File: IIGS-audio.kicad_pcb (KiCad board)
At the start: 2 copper layers, 65.8 x 46.6 mm, 39 parts, among them J1 Conn_01x07, J2 Conn_01x02_Male, J3 SJ1-3515N, J4 AppleII_slot, U1 74HC4052D, U2 TL074

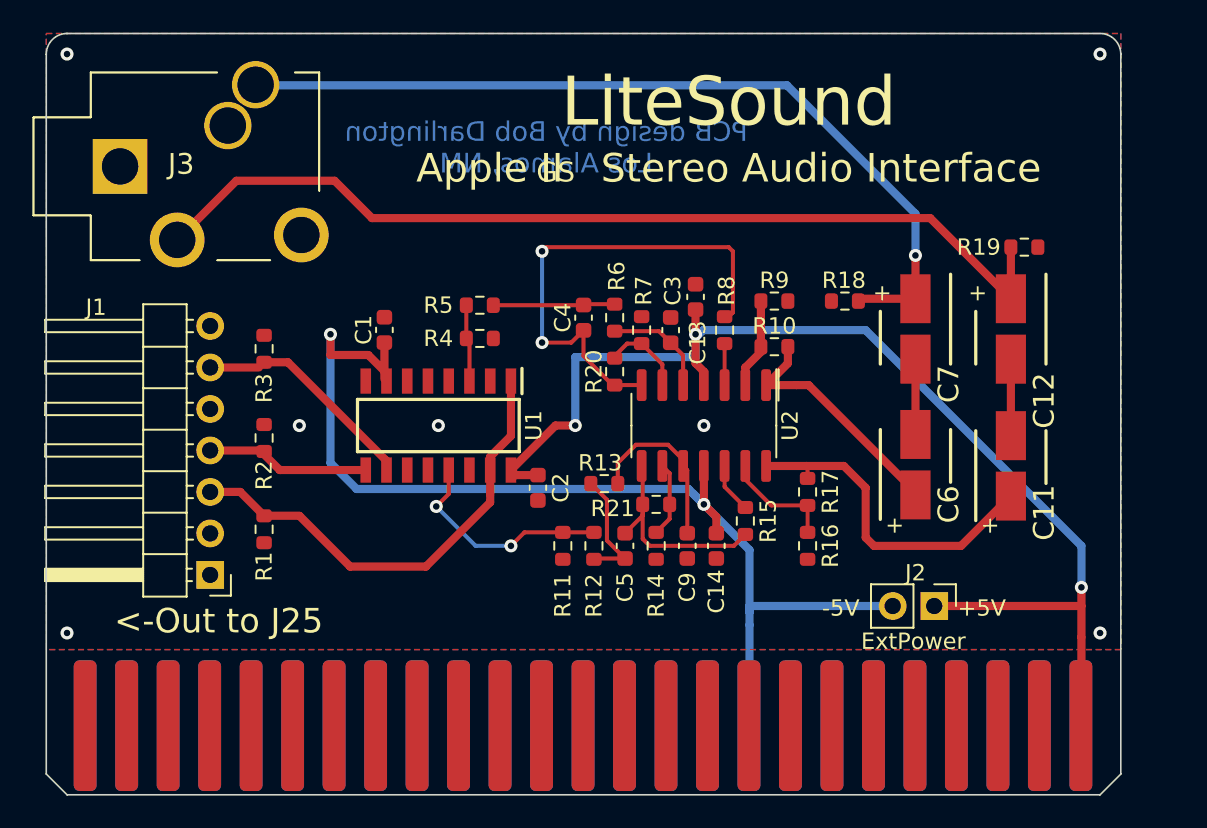
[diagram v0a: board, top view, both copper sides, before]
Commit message: Minor layout tweaks.
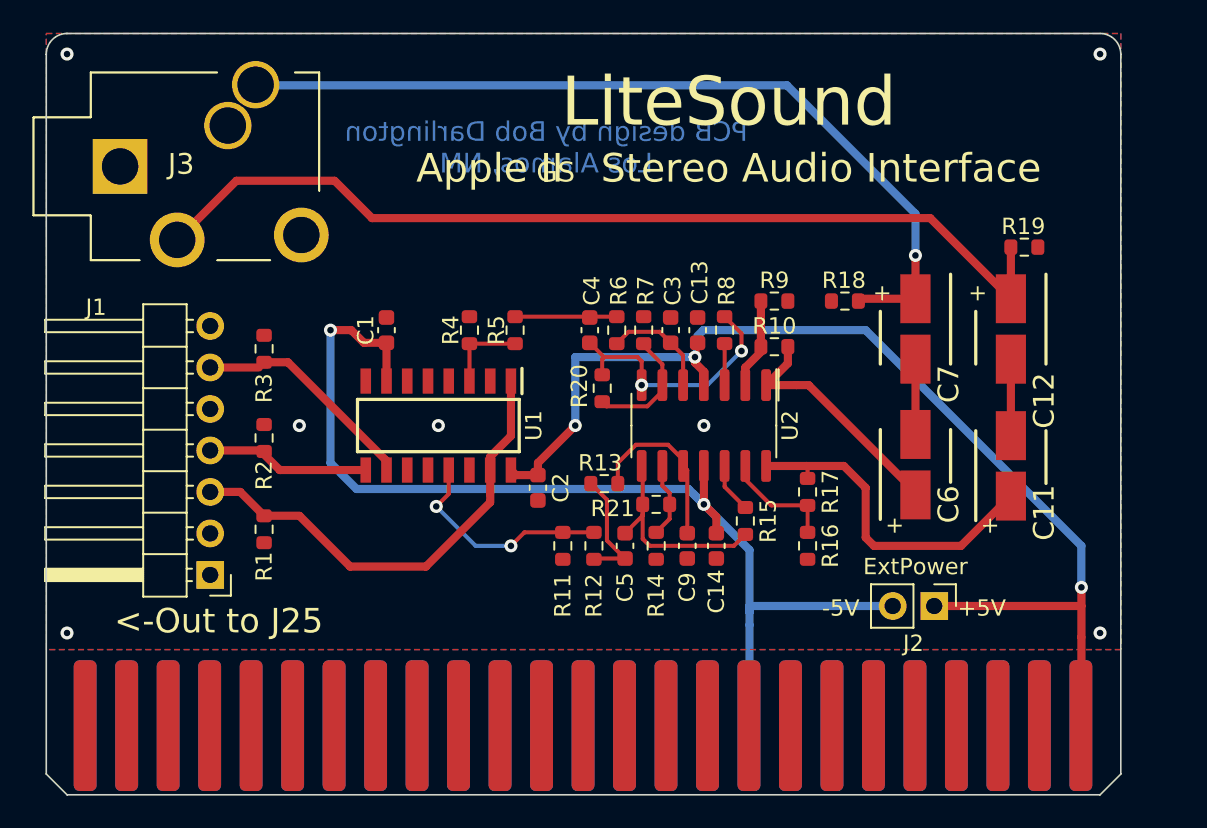
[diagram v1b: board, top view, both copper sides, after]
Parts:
- moved R5 2.64 mm to (139.8, 101.7), turned to 90 degrees
- moved C13 2.04 mm to (151.0, 101.7)
- moved R20 1.27 mm to (145.2, 105.3), turned to -90 degrees
- moved C4 0.85 mm to (144.4, 101.7)
- moved R4 0.81 mm to (137.0, 101.7), turned to -90 degrees
- moved R6 0.77 mm to (146.1, 101.7)
- moved C1 0.13 mm to (132.0, 101.7)
- moved R7 0.13 mm to (147.7, 101.7)
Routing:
- net Net-(C4-Pad2): track 30.7 -> 15.7 mm
- net +5V: track 74.0 -> 70.7 mm
- net Net-(R20-Pad2): track 5.21 -> 7.35 mm
- net -5V: track 69.0 -> 67.3 mm
- net Net-(C4-Pad1): track 7.46 -> 6.26 mm

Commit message: Minor tweaks to layout
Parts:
- moved R16 2.03 mm to (155.7, 114.9)
- moved R17 0.46 mm to (157.4, 111.9)
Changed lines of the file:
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@@
   )
   (footprint "Resistor_SMD:R_0603_1608Metric" (layer "F.Cu")
-    (at 157.734 114.9325 -90)
-    (descr "Resistor SMD 0603 (1608 Metric), square (rectangular) end terminal, IPC_7351 nominal, (Body size source: IPC-SM-782 page 72, https://www.pcb-3d.com/wordpress/wp-content/uploads/ipc-sm-782a_amendment_1_and_2.pdf), generated with kicad-footprint-generator")
-    (tags "resistor")
-    (property "Sheetfile" "IIGS-audio.kicad_sch")
-    (property "Sheetname" "")
-    (attr smd)
-    (fp_text reference "R16" (at 0 -1.397 90) (layer "F.SilkS")
+    (at 155.702 114.935 -90)
+    (descr "Resistor SMD 0603 (1608 Metric), square (rectangular) end terminal, IPC_7351 nominal, (Body size source: IPC-SM-782 page 72, https://www.pcb-3d.com/wordpress/wp-content/uploads/ipc-sm-782a_amendment_1_and_2.pdf), generated with kicad-footprint-generator")
+    (tags "resistor")
+    (property "Sheetfile" "IIGS-audio.kicad_sch")
+    (property "Sheetname" "")
+    (attr smd)
+    (fp_text reference "R16" (at 2.921 0 90) (layer "F.SilkS")
       (effects (font (size 1 1) (thickness 0.15)))
     )
@@
     (property "Sheetname" "")
     (attr smd)
-    (fp_text reference "R15" (at 0 1.397 90) (layer "F.SilkS")
+    (fp_text reference "R15" (at -2.9235 0 90) (layer "F.SilkS")
       (effects (font (size 1 1) (thickness 0.15)))
     )
@@
   )
   (footprint "Resistor_SMD:R_0603_1608Metric" (layer "F.Cu")
-    (at 157.734 111.6305 90)
+    (at 157.353 111.887 90)
     (descr "Resistor SMD 0603 (1608 Metric), square (rectangular) end terminal, IPC_7351 nominal, (Body size source: IPC-SM-782 page 72, https://www.pcb-3d.com/wordpress/wp-content/uploads/ipc-sm-782a_amendment_1_and_2.pdf), generated with kicad-footprint-generator")
     (tags "resistor")
@@
   (segment (start 152.654 110.0415) (end 152.654 111.3135) (width 0.25) (layer "F.Cu") (net 73))
   (segment (start 164.338 108.1845) (end 164.338 103.5025) (width 0.5) (layer "F.Cu") (net 74))
-  (segment (start 155.511 112.4555) (end 157.734 112.4555) (width 0.25) (layer "F.Cu") (net 75))
-  (segment (start 157.734 112.4555) (end 157.734 114.1075) (width 0.25) (layer "F.Cu") (net 75))
-  (segment (start 153.924 110.8685) (end 155.511 112.4555) (width 0.25) (layer "F.Cu") (net 75))
-  (segment (start 153.924 110.0415) (end 153.924 110.8685) (width 0.25) (layer "F.Cu") (net 75))
+  (segment (start 155.702 114.11) (end 155.702 112.776) (width 0.25) (layer "F.Cu") (net 75))
+  (segment (start 157.29 112.649) (end 155.702 112.649) (width 0.25) (layer "F.Cu") (net 75))
+  (segment (start 155.702 112.649) (end 155.702 112.776) (width 0.25) (layer "F.Cu") (net 75))
+  (segment (start 153.924 110.871) (end 155.702 112.649) (width 0.25) (layer "F.Cu") (net 75))
+  (segment (start 153.924 110.0415) (end 153.924 110.871) (width 0.25) (layer "F.Cu") (net 75))
+  (segment (start 157.353 112.712) (end 157.29 112.649) (width 0.25) (layer "F.Cu") (net 75))
   (segment (start 170.18 103.5025) (end 170.18 108.1845) (width 0.5) (layer "F.Cu") (net 76))
   (segment (start 156.527 103.7585) (end 155.194 105.0915) (width 0.5) (layer "F.Cu") (net 77))
@@
   (segment (start 156.527 102.7405) (end 156.527 103.7585) (width 0.5) (layer "F.Cu") (net 77))
   (segment (start 164.338 111.8125) (end 163.758 111.8125) (width 0.25) (layer "F.Cu") (net 77))
-  (segment (start 157.734 110.8055) (end 157.734 110.1065) (width 0.25) (layer "F.Cu") (net 78))
+  (segment (start 157.4125 110.0415) (end 157.0315 110.0415) (width 0.5) (layer "F.Cu") (net 78))
   (segment (start 161.29 114.4245) (end 161.29 111.3765) (width 0.5) (layer "F.Cu") (net 78))
   (segment (start 159.955 110.0415) (end 157.669 110.0415) (width 0.5) (layer "F.Cu") (net 78))
-  (segment (start 157.734 110.1065) (end 157.669 110.0415) (width 0.25) (layer "F.Cu") (net 78))
+  (segment (start 157.669 110.0415) (end 157.4125 110.0415) (width 0.5) (layer "F.Cu") (net 78))
+  (segment (start 157.353 110.0415) (end 157.353 111.062) (width 0.5) (layer "F.Cu") (net 78))
   (segment (start 161.798 114.9325) (end 161.29 114.4245) (width 0.5) (layer "F.Cu") (net 78))
   (segment (start 167.132 114.9325) (end 161.798 114.9325) (width 0.5) (layer "F.Cu") (net 78))
-  (segment (start 157.669 110.0415) (end 155.194 110.0415) (width 0.5) (layer "F.Cu") (net 78))
+  (segment (start 157.0315 110.0415) (end 155.194 110.0415) (width 0.5) (layer "F.Cu") (net 78))
   (segment (start 161.29 111.3765) (end 159.955 110.0415) (width 0.5) (layer "F.Cu") (net 78))
   (segment (start 170.18 111.8845) (end 167.132 114.9325) (width 0.5) (layer "F.Cu") (net 78))
